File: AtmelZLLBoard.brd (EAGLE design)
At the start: 28.9 x 29.2 mm, 9 parts

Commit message: Replaced resistors
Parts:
- R1, R2, R3: device resistor:0207/7 -> resistor:0204/5
- moved U$2 1.80 mm to (10.2, 6.35)
- moved R1 1.27 mm to (15.2, 7.62)
- moved R3 1.27 mm to (15.2, 2.54)
- moved R2 1.27 mm to (15.2, 5.08)
- moved U$1 1.27 mm to (6.35, 11.4)
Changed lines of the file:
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@@
 </autorouter>
 <elements>
-<element name="U$1" library="atmel-zll" package="ATSAMR21B18-MZ210PA" value="ATSAMR21B18-MZ210PA" x="6.35" y="12.7"/>
-<element name="U$2" library="osram_led" package="LRTB_GFTG" value="LRTB_GFTG" x="8.89" y="7.62" rot="R270"/>
-<element name="R1" library="resistor" package="0207/7" value="5.6R" x="15.24" y="8.89" smashed="yes" rot="R180">
-<attribute name="NAME" x="12.827" y="9.652" size="1.016" layer="25" ratio="10" rot="R270"/>
-<attribute name="VALUE" x="17.526" y="9.4488" size="1.27" layer="27" ratio="10" rot="R180"/>
+<element name="U$1" library="atmel-zll" package="ATSAMR21B18-MZ210PA" value="ATSAMR21B18-MZ210PA" x="6.35" y="11.43"/>
+<element name="U$2" library="osram_led" package="LRTB_GFTG" value="LRTB_GFTG" x="10.16" y="6.35" rot="R270"/>
+<element name="R1" library="resistor" package="0204/5" value="5.6R" x="15.24" y="7.62" smashed="yes" rot="R180">
+<attribute name="NAME" x="14.478" y="7.747" size="1.016" layer="25" ratio="10" align="center"/>
 </element>
-<element name="R2" library="resistor" package="0207/7" value="5.6R" x="15.24" y="6.35" smashed="yes" rot="R180">
-<attribute name="NAME" x="12.827" y="7.112" size="1.016" layer="25" ratio="10" rot="R270"/>
-<attribute name="VALUE" x="17.526" y="6.9088" size="1.27" layer="27" ratio="10" rot="R180"/>
+<element name="R2" library="resistor" package="0204/5" value="5.6R" x="15.24" y="5.08" smashed="yes" rot="R180">
+<attribute name="NAME" x="14.478" y="5.207" size="1.016" layer="25" ratio="10" align="center"/>
 </element>
-<element name="R3" library="resistor" package="0207/7" value="68" x="15.24" y="3.81" smashed="yes" rot="R180">
-<attribute name="NAME" x="12.827" y="4.572" size="1.016" layer="25" ratio="10" rot="R270"/>
-<attribute name="VALUE" x="17.526" y="4.3688" size="1.27" layer="27" ratio="10" rot="R180"/>
+<element name="R3" library="resistor" package="0204/5" value="68" x="15.24" y="2.54" smashed="yes" rot="R180">
+<attribute name="NAME" x="14.478" y="2.667" size="1.016" layer="25" ratio="10" align="center"/>
 </element>
 <element name="JP1" library="pinhead" package="1X02" value="" x="2.54" y="6.35" rot="R270"/>

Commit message: Rewired stuff, added extra via's. Changed board dimensions.
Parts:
- moved JP2 3.59 mm to (24.1, 10.2)
- moved U$3 1.27 mm to (20.3, 12.7)
- moved JP1 1.27 mm to (2.54, 5.08)
- moved JP5 1.27 mm to (22.9, 5.08)
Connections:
- removed net N$1: JP5.2, U$1.3
- new net N$7: JP5.6, U$1.3
- net N$6: now also JP5.2; no longer JP5.6
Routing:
- net N$7: track 0.00 -> 19.3 mm
- net N$1: track 15.3 -> 0.00 mm
- net N$6: track 23.0 -> 9.71 mm
- net N$5: track 18.8 -> 15.2 mm
- net PA19: track 10.0 -> 6.95 mm
- net R: track 2.54 -> 3.81 mm
- net G: track 2.54 -> 3.81 mm
- net B: track 2.54 -> 3.81 mm
- net GND: track 5.90 -> 7.17 mm, vias 6 -> 77
- net N$4: track 2.92 -> 3.88 mm
- net N$2: track 3.27 -> 4.02 mm
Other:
- board size 28.9 x 29.2 mm -> 26.3 x 27.9 mm

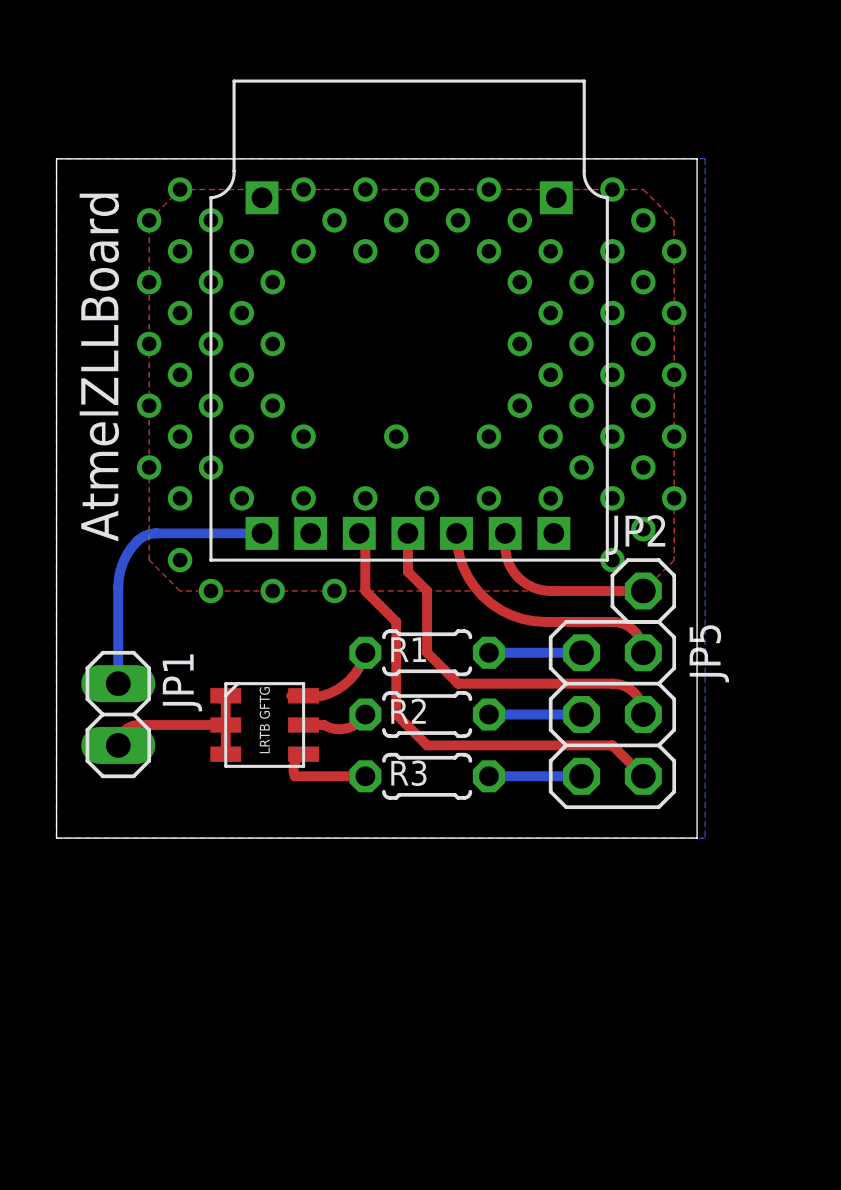
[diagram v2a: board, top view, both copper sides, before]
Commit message: Replaced the regalar module with the module that contains the dev pads. Decreased the pad size, added oshpark rules for DRC. Added extra header onto the board that routes the programming pins.
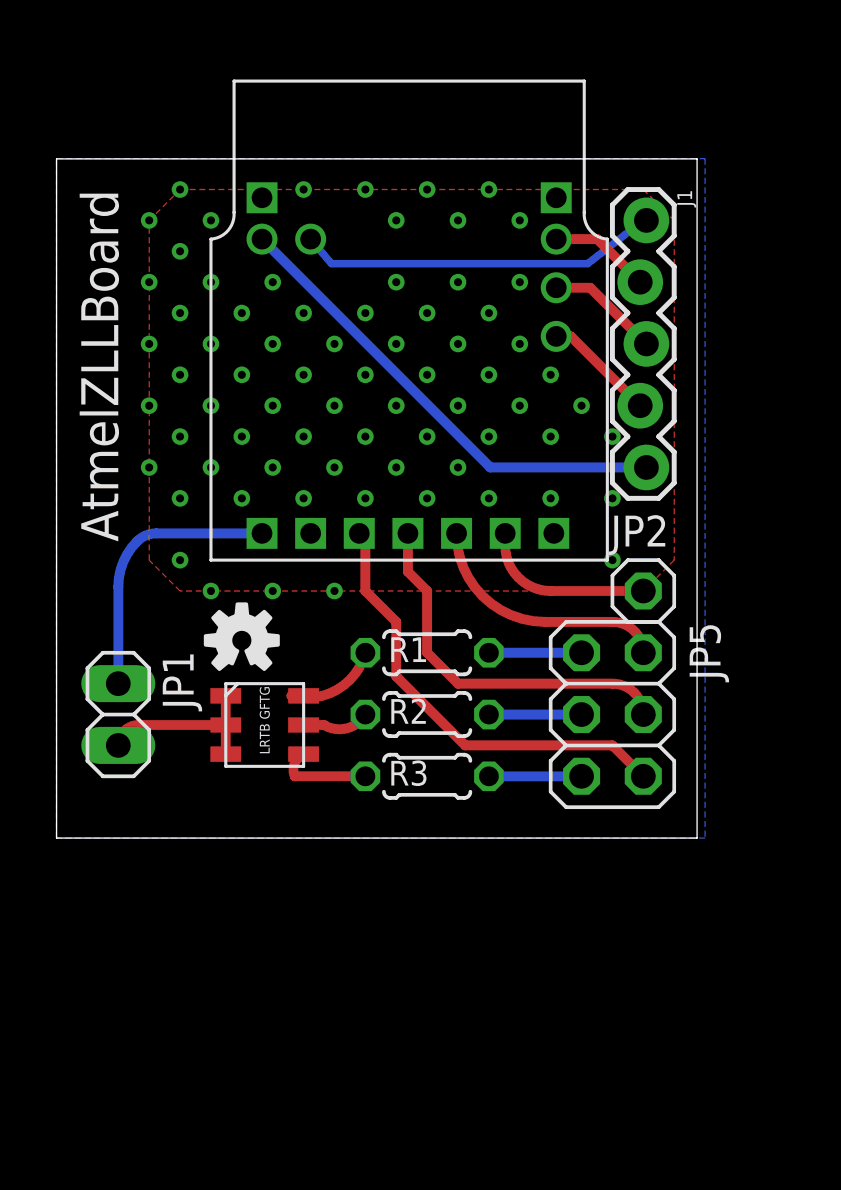
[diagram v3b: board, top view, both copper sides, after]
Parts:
- added J1: (no value), SparkFun-Connectors:1X05_LOCK
- added U$4: (no value), tiwtie:TIWTIE_LOGO
- U$1: value ATSAMR21B18-MZ210PA -> ATSAMR21B18-MZ210PA-DEV; device atmel-zll:ATSAMR21B18-MZ210PA -> atmel-zll:ATSAMR21B18-MZ210PA-DEV
- U$3: device NBitWonder:OSHW1 -> SparkFun-Aesthetics:OSHW-LOGO-S
- moved U$3 13.5 mm to (7.62, 8.13), flipped to the top
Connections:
- new net N$1: J1.5, U$1.TP1
- new net N$10: J1.2, U$1.TP4
- new net N$11: J1.1, U$1.TP5
- new net N$8: J1.4, U$1.TP2
- new net N$9: J1.3, U$1.TP3
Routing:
- net N$1: track 0.00 -> 19.7 mm
- net N$11: track 0.00 -> 14.8 mm
- net N$9: track 0.00 -> 4.66 mm
- net N$8: track 0.00 -> 4.63 mm
- net N$10: track 0.00 -> 4.19 mm
- net N$7: track 19.3 -> 18.4 mm
- net GND: vias 77 -> 72
